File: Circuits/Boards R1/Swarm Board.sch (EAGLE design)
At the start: 93 parts, among them CON1 ISP(2X3), T1 NPN2N2222, T10 TEFT4300, T11 NPN2N2222, T13 NPN2N2222, T14 NPN2N2222, T15 NPN2N2222, T16 NPN2N2222, T17 NPN2N2222, T18 NPN2N2222, T2 NPN2N2222, T3 NPN2N2222, T4 TEFT4300, T5 TEFT4300, T6 TEFT4300, T7 TEFT4300, T8 TEFT4300, T9 TEFT4300, U1 ATMEGA324P, U3 TB6552FN/FNG

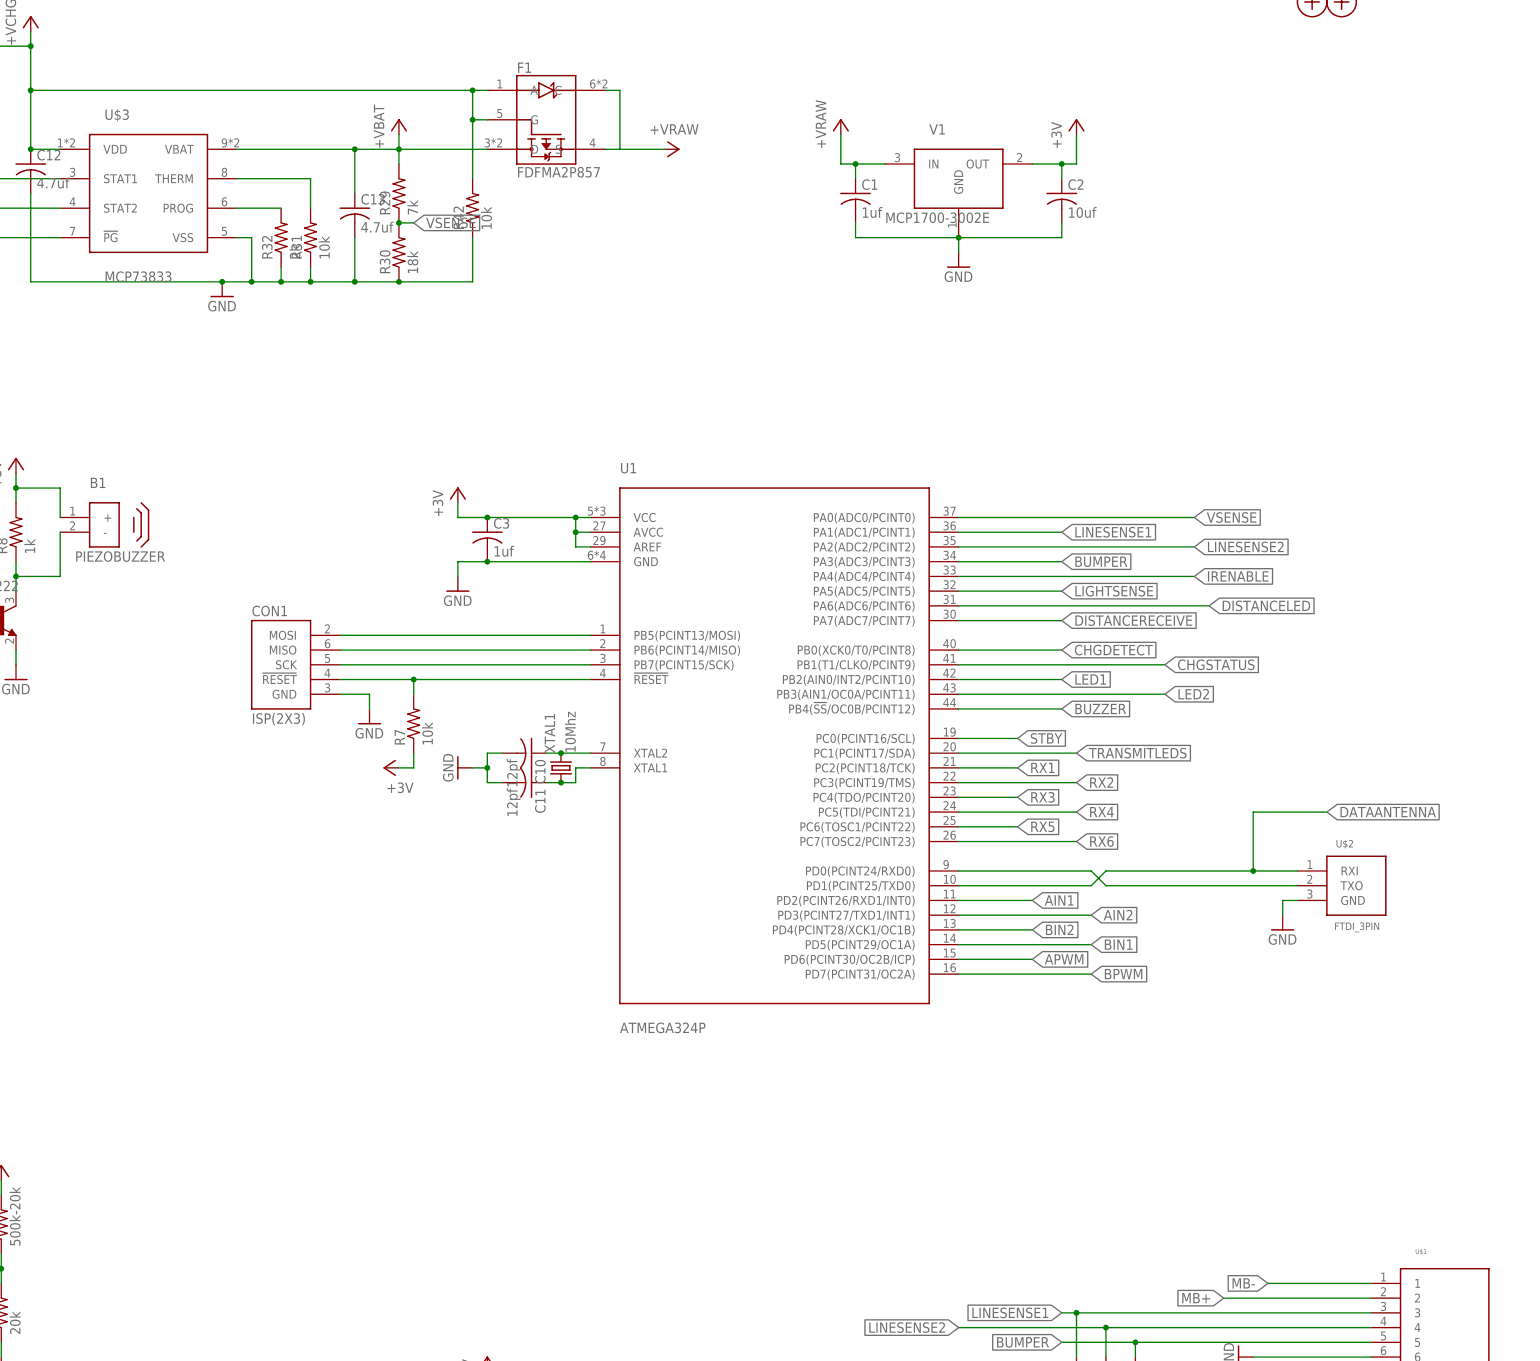
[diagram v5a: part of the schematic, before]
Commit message: 
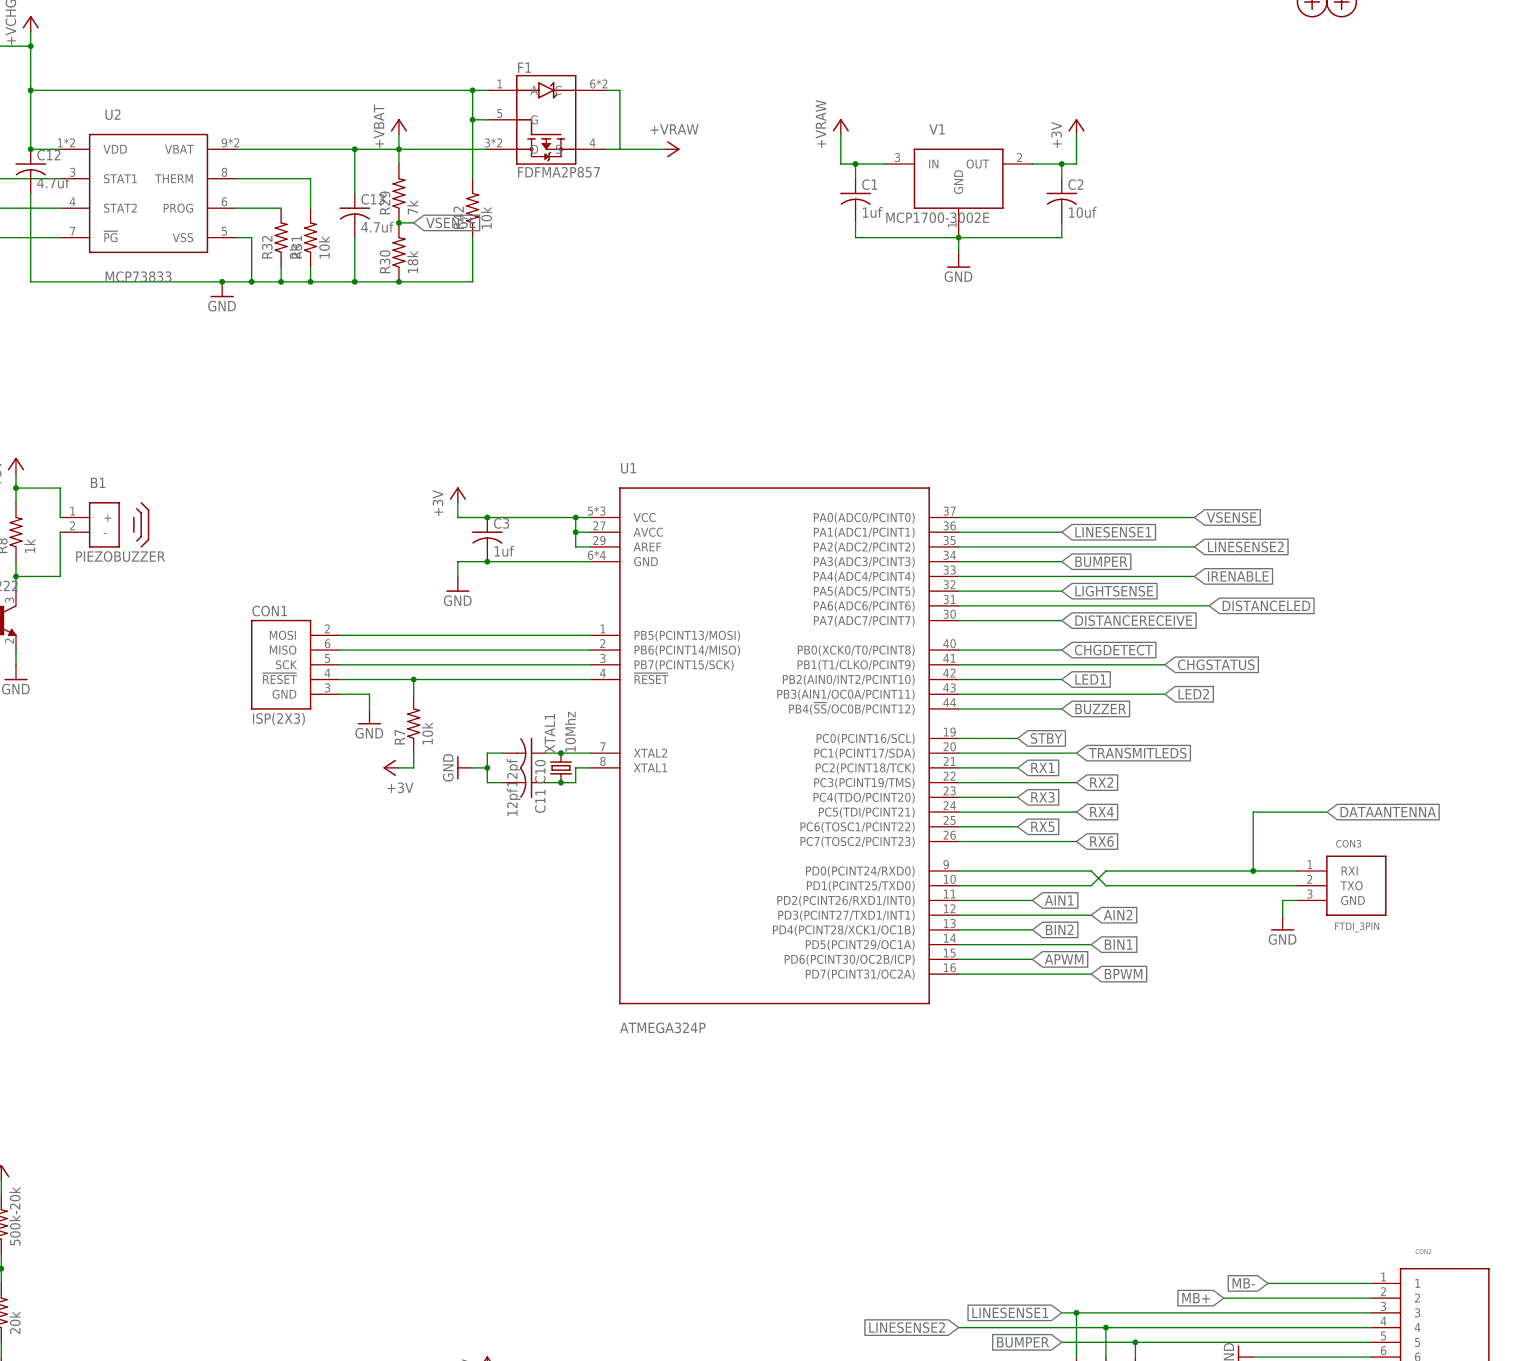
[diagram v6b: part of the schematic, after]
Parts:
- renumbered U$1 to CON2, U$2 to CON3, U$3 to U2
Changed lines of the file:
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@@
 <part name="R26" library="Passive" deviceset="RES" device="0603" value="750"/>
 <part name="R28" library="Passive" deviceset="RES" device="0603" value="1k"/>
-<part name="U$1" library="Mechanical" deviceset="MAIN_CONNECTOR" device=""/>
-<part name="U$2" library="Mechanical" deviceset="FTDI_3PIN" device=""/>
+<part name="CON2" library="Mechanical" deviceset="MAIN_CONNECTOR" device=""/>
+<part name="CON3" library="Mechanical" deviceset="FTDI_3PIN" device=""/>
 <part name="P+15" library="Supply" deviceset="+VCHG" device=""/>
 <part name="GND18" library="Supply" deviceset="GND" device=""/>
@@
 <part name="GND20" library="Supply" deviceset="GND" device=""/>
 <part name="P+3" library="Supply" deviceset="+3V" device=""/>
-<part name="U$3" library="PowerIC" deviceset="MCP73833" device=""/>
+<part name="U2" library="PowerIC" deviceset="MCP73833" device=""/>
 <part name="R29" library="Passive" deviceset="RES" device="0603" value="7k"/>
 <part name="R30" library="Passive" deviceset="RES" device="0603" value="18k"/>
@@
 <instance part="R26" gate="G$1" x="-160.02" y="-35.56" rot="R90"/>
 <instance part="R28" gate="G$1" x="-144.78" y="20.32"/>
-<instance part="U$1" gate="G$1" x="114.3" y="-106.68"/>
-<instance part="U$2" gate="G$1" x="99.06" y="-25.4"/>
+<instance part="CON2" gate="G$1" x="114.3" y="-106.68"/>
+<instance part="CON3" gate="G$1" x="99.06" y="-25.4"/>
 <instance part="P+15" gate="G$1" x="-251.46" y="-43.18" rot="R270"/>
 <instance part="GND18" gate="1" x="-248.92" y="-68.58" rot="R90"/>
@@
 <instance part="GND20" gate="1" x="96.52" y="-114.3" rot="R270"/>
 <instance part="P+3" gate="1" x="71.12" y="-111.76" rot="R90"/>
-<instance part="U$3" gate="G$1" x="-114.3" y="93.98"/>
+<instance part="U2" gate="G$1" x="-114.3" y="93.98"/>
 <instance part="R29" gate="G$1" x="-66.04" y="93.98" rot="R90"/>
 <instance part="R30" gate="G$1" x="-66.04" y="83.82" rot="R90"/>
@@
 </segment>
 <segment>
-<pinref part="U$1" gate="G$1" pin="8"/>
+<pinref part="CON2" gate="G$1" pin="8"/>
 <wire x1="101.6" y1="-111.76" x2="81.28" y2="-111.76" width="0.1524" layer="91"/>
 <pinref part="P+3" gate="1" pin="+3V"/>
@@
 <wire x1="86.36" y1="-27.94" x2="86.36" y2="-30.48" width="0.1524" layer="91"/>
 <pinref part="GND5" gate="1" pin="GND"/>
-<pinref part="U$2" gate="G$1" pin="GND"/>
+<pinref part="CON3" gate="G$1" pin="GND"/>
 </segment>
 <segment>
@@
 </segment>
 <segment>
-<pinref part="U$1" gate="G$1" pin="6"/>
+<pinref part="CON2" gate="G$1" pin="6"/>
 <wire x1="101.6" y1="-106.68" x2="81.28" y2="-106.68" width="0.1524" layer="91"/>
 <pinref part="GND28" gate="1" pin="GND"/>
@@
 </segment>
 <segment>
-<pinref part="U$1" gate="G$1" pin="9"/>
+<pinref part="CON2" gate="G$1" pin="9"/>
 <wire x1="101.6" y1="-114.3" x2="99.06" y2="-114.3" width="0.1524" layer="91"/>
 <pinref part="GND20" gate="1" pin="GND"/>
@@
 <wire x1="-96.52" y1="78.74" x2="-91.44" y2="78.74" width="0.1524" layer="91"/>
 <wire x1="-91.44" y1="78.74" x2="-86.36" y2="78.74" width="0.1524" layer="91"/>
-<pinref part="U$3" gate="G$1" pin="VSS"/>
+<pinref part="U2" gate="G$1" pin="VSS"/>
 <wire x1="-86.36" y1="78.74" x2="-81.28" y2="78.74" width="0.1524" layer="91"/>
 <wire x1="-81.28" y1="78.74" x2="-73.66" y2="78.74" width="0.1524" layer="91"/>
@@
 <net name="+VBAT" class="0">
 <segment>
-<pinref part="U$1" gate="G$1" pin="7"/>
+<pinref part="CON2" gate="G$1" pin="7"/>
 <wire x1="101.6" y1="-109.22" x2="76.2" y2="-109.22" width="0.1524" layer="91"/>
 <label x="76.2" y="-109.22" size="1.778" layer="91" rot="R180" xref="yes"/>
@@
 <wire x1="-66.04" y1="101.6" x2="-50.8" y2="101.6" width="0.1524" layer="91"/>
 <junction x="-66.04" y="101.6"/>
-<pinref part="U$3" gate="G$1" pin="VBAT"/>
+<pinref part="U2" gate="G$1" pin="VBAT"/>
 <wire x1="-93.98" y1="101.6" x2="-73.66" y2="101.6" width="0.1524" layer="91"/>
 <junction x="-73.66" y="101.6"/>
@@
 </segment>
 <segment>
-<pinref part="U$3" gate="G$1" pin="VDD"/>
+<pinref part="U2" gate="G$1" pin="VDD"/>
 <wire x1="-124.46" y1="101.6" x2="-129.54" y2="101.6" width="0.1524" layer="91"/>
 <wire x1="-129.54" y1="101.6" x2="-129.54" y2="111.76" width="0.1524" layer="91"/>
@@
 <net name="CHGDETECT" class="0">
 <segment>
-<pinref part="U$3" gate="G$1" pin="!PG"/>
+<pinref part="U2" gate="G$1" pin="!PG"/>
 <wire x1="-124.46" y1="86.36" x2="-139.7" y2="86.36" width="0.1524" layer="91"/>
 <label x="-139.7" y="86.36" size="1.778" layer="91" rot="R180" xref="yes"/>
@@
 </segment>
 <segment>
-<pinref part="U$1" gate="G$1" pin="3"/>
+<pinref part="CON2" gate="G$1" pin="3"/>
 <label x="48.26" y="-99.06" size="1.778" layer="91" rot="R180" xref="yes"/>
 <wire x1="50.8" y1="-99.06" x2="48.26" y2="-99.06" width="0.1524" layer="91"/>
@@
 </segment>
 <segment>
-<pinref part="U$1" gate="G$1" pin="4"/>
+<pinref part="CON2" gate="G$1" pin="4"/>
 <label x="30.48" y="-101.6" size="1.778" layer="91" rot="R180" xref="yes"/>
 <wire x1="55.88" y1="-101.6" x2="53.34" y2="-101.6" width="0.1524" layer="91"/>
@@
 <pinref part="U1" gate="G$1" pin="PD1(PCINT25/TXD0)"/>
 <wire x1="53.34" y1="-25.4" x2="30.48" y2="-25.4" width="0.1524" layer="91"/>
-<pinref part="U$2" gate="G$1" pin="RXI"/>
+<pinref part="CON3" gate="G$1" pin="RXI"/>
 <wire x1="81.28" y1="-22.86" x2="81.28" y2="-12.7" width="0.1524" layer="91"/>
 <wire x1="81.28" y1="-12.7" x2="93.98" y2="-12.7" width="0.1524" layer="91"/>
@@
 <wire x1="53.34" y1="-22.86" x2="55.88" y2="-25.4" width="0.1524" layer="91"/>
 <wire x1="55.88" y1="-25.4" x2="88.9" y2="-25.4" width="0.1524" layer="91"/>
-<pinref part="U$2" gate="G$1" pin="TXO"/>
+<pinref part="CON3" gate="G$1" pin="TXO"/>
 </segment>
 </net>
@@
 </segment>
 <segment>
-<pinref part="U$1" gate="G$1" pin="12"/>
+<pinref part="CON2" gate="G$1" pin="12"/>
 <wire x1="101.6" y1="-121.92" x2="96.52" y2="-124.46" width="0.1524" layer="91"/>
 <label x="96.52" y="-124.46" size="1.778" layer="91" rot="R180" xref="yes"/>
@@
 </segment>
 <segment>
-<pinref part="U$1" gate="G$1" pin="11"/>
+<pinref part="CON2" gate="G$1" pin="11"/>
 <wire x1="101.6" y1="-119.38" x2="99.06" y2="-119.38" width="0.1524" layer="91"/>
 <label x="99.06" y="-119.38" size="1.778" layer="91" rot="R180" xref="yes"/>
@@
 </segment>
 <segment>
-<pinref part="U$1" gate="G$1" pin="2"/>
+<pinref part="CON2" gate="G$1" pin="2"/>
 <wire x1="101.6" y1="-96.52" x2="76.2" y2="-96.52" width="0.1524" layer="91"/>
 <label x="76.2" y="-96.52" size="1.778" layer="91" rot="R180" xref="yes"/>
@@
 </segment>
 <segment>
-<pinref part="U$1" gate="G$1" pin="1"/>
+<pinref part="CON2" gate="G$1" pin="1"/>
 <wire x1="101.6" y1="-93.98" x2="83.82" y2="-93.98" width="0.1524" layer="91"/>
 <label x="83.82" y="-93.98" size="1.778" layer="91" rot="R180" xref="yes"/>
@@
 <net name="CHGSTATUS" class="0">
 <segment>
-<pinref part="U$3" gate="G$1" pin="STAT2"/>
+<pinref part="U2" gate="G$1" pin="STAT2"/>
 <wire x1="-124.46" y1="91.44" x2="-139.7" y2="91.44" width="0.1524" layer="91"/>
 <label x="-139.7" y="91.44" size="1.778" layer="91" rot="R180" xref="yes"/>
@@
 </segment>
 <segment>
-<pinref part="U$1" gate="G$1" pin="5"/>
+<pinref part="CON2" gate="G$1" pin="5"/>
 <label x="48.26" y="-104.14" size="1.778" layer="91" rot="R180" xref="yes"/>
 <wire x1="60.96" y1="-104.14" x2="48.26" y2="-104.14" width="0.1524" layer="91"/>
@@
 <net name="N$28" class="0">
 <segment>
-<pinref part="U$3" gate="G$1" pin="PROG"/>
+<pinref part="U2" gate="G$1" pin="PROG"/>
 <pinref part="R32" gate="G$1" pin="2"/>
 <wire x1="-93.98" y1="91.44" x2="-86.36" y2="91.44" width="0.1524" layer="91"/>
@@
 <net name="N$33" class="0">
 <segment>
-<pinref part="U$3" gate="G$1" pin="STAT1"/>
+<pinref part="U2" gate="G$1" pin="STAT1"/>
 <wire x1="-124.46" y1="96.52" x2="-139.7" y2="96.52" width="0.1524" layer="91"/>
 <pinref part="R1" gate="G$1" pin="1"/>
@@
 <net name="N$22" class="0">
 <segment>
-<pinref part="U$3" gate="G$1" pin="THERM"/>
+<pinref part="U2" gate="G$1" pin="THERM"/>
 <pinref part="R31" gate="G$1" pin="2"/>
 <wire x1="-93.98" y1="96.52" x2="-81.28" y2="96.52" width="0.1524" layer="91"/>
@@
 <net name="N$7" class="0">
 <segment>
-<pinref part="U$1" gate="G$1" pin="10"/>
+<pinref part="CON2" gate="G$1" pin="10"/>
 <wire x1="101.6" y1="-116.84" x2="83.82" y2="-116.84" width="0.1524" layer="91"/>
 <wire x1="83.82" y1="-116.84" x2="83.82" y2="-124.46" width="0.1524" layer="91"/>
